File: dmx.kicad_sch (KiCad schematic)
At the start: 18 parts, among them J1 Conn_01x15_Socket, J2 Conn_01x04_Pin, J3 Conn_01x15_Socket, J5 Barrel_Jack_MountingPin, SW1 SW_Push, SW3 SW_Push

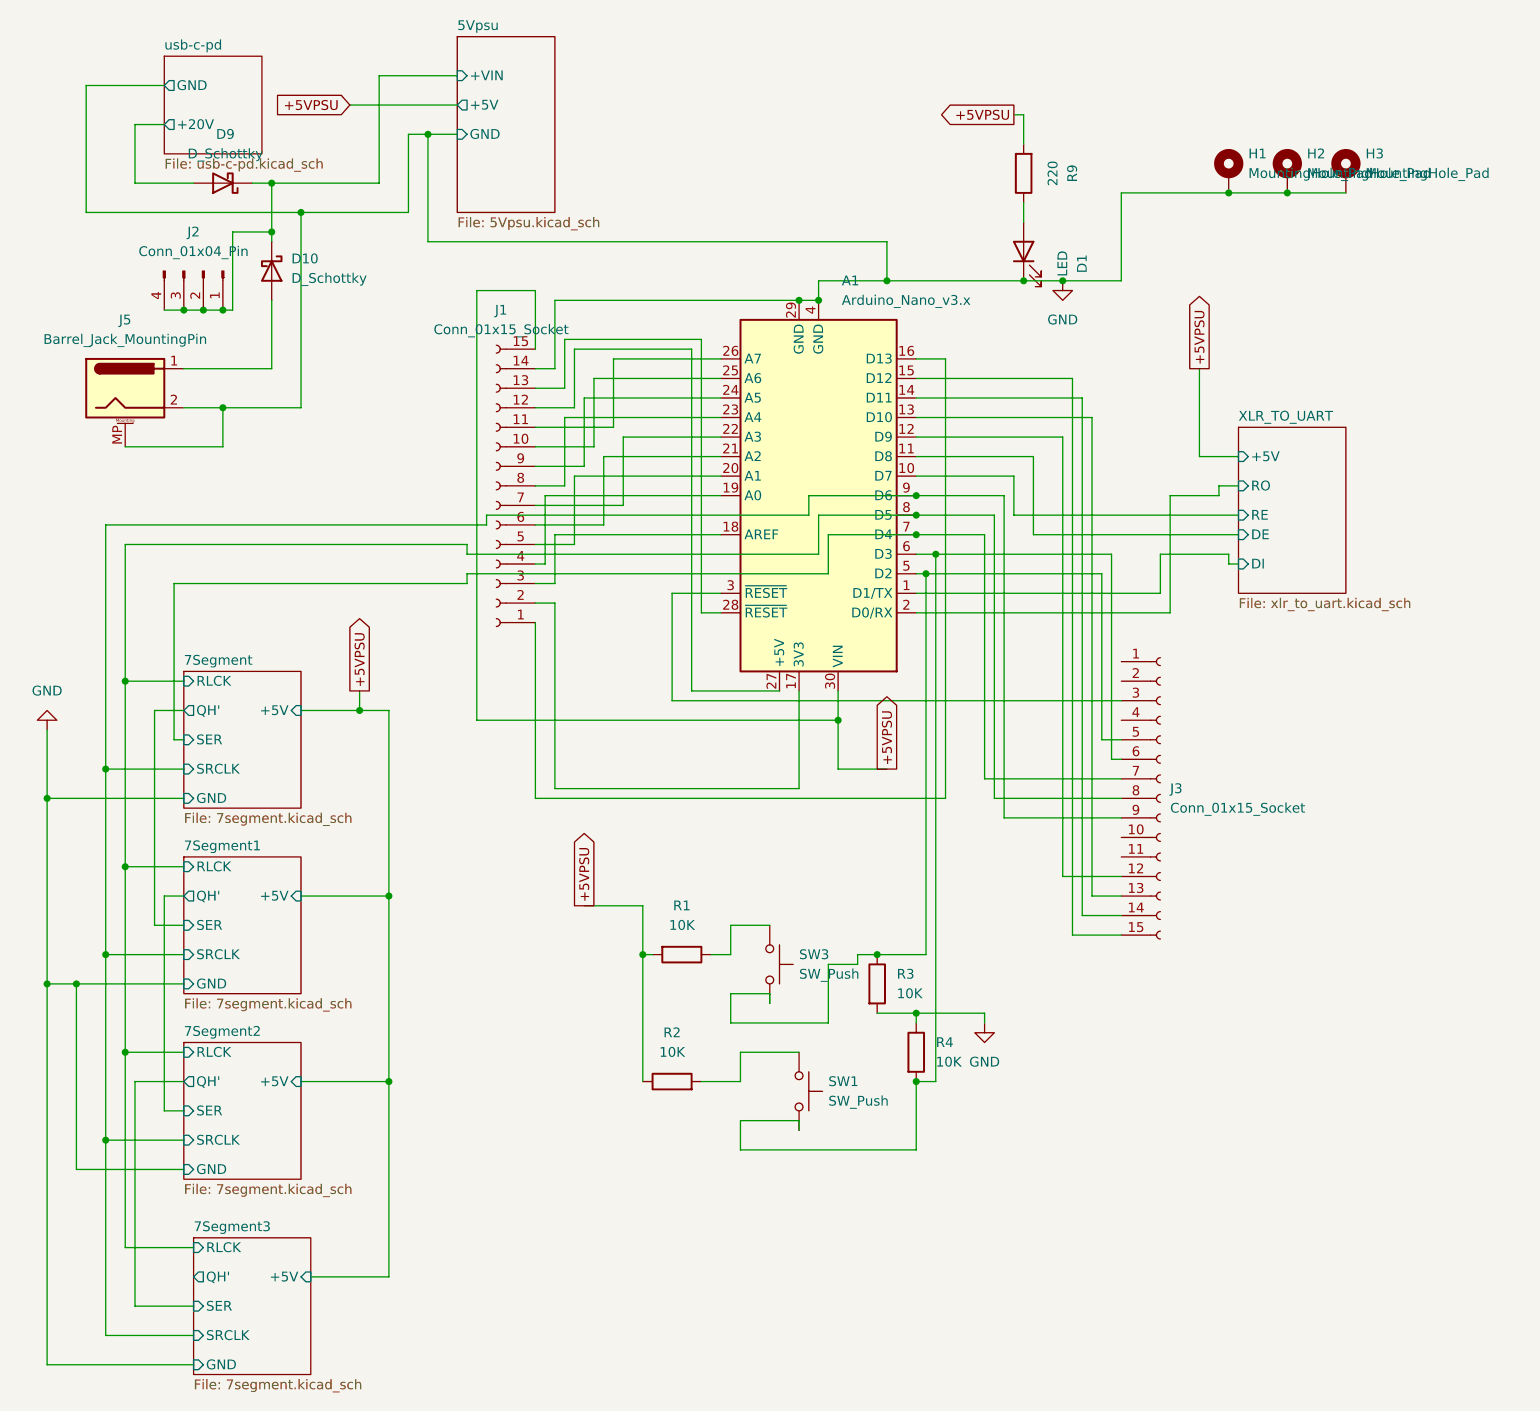
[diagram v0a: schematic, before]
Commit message: switch to cheaper components.
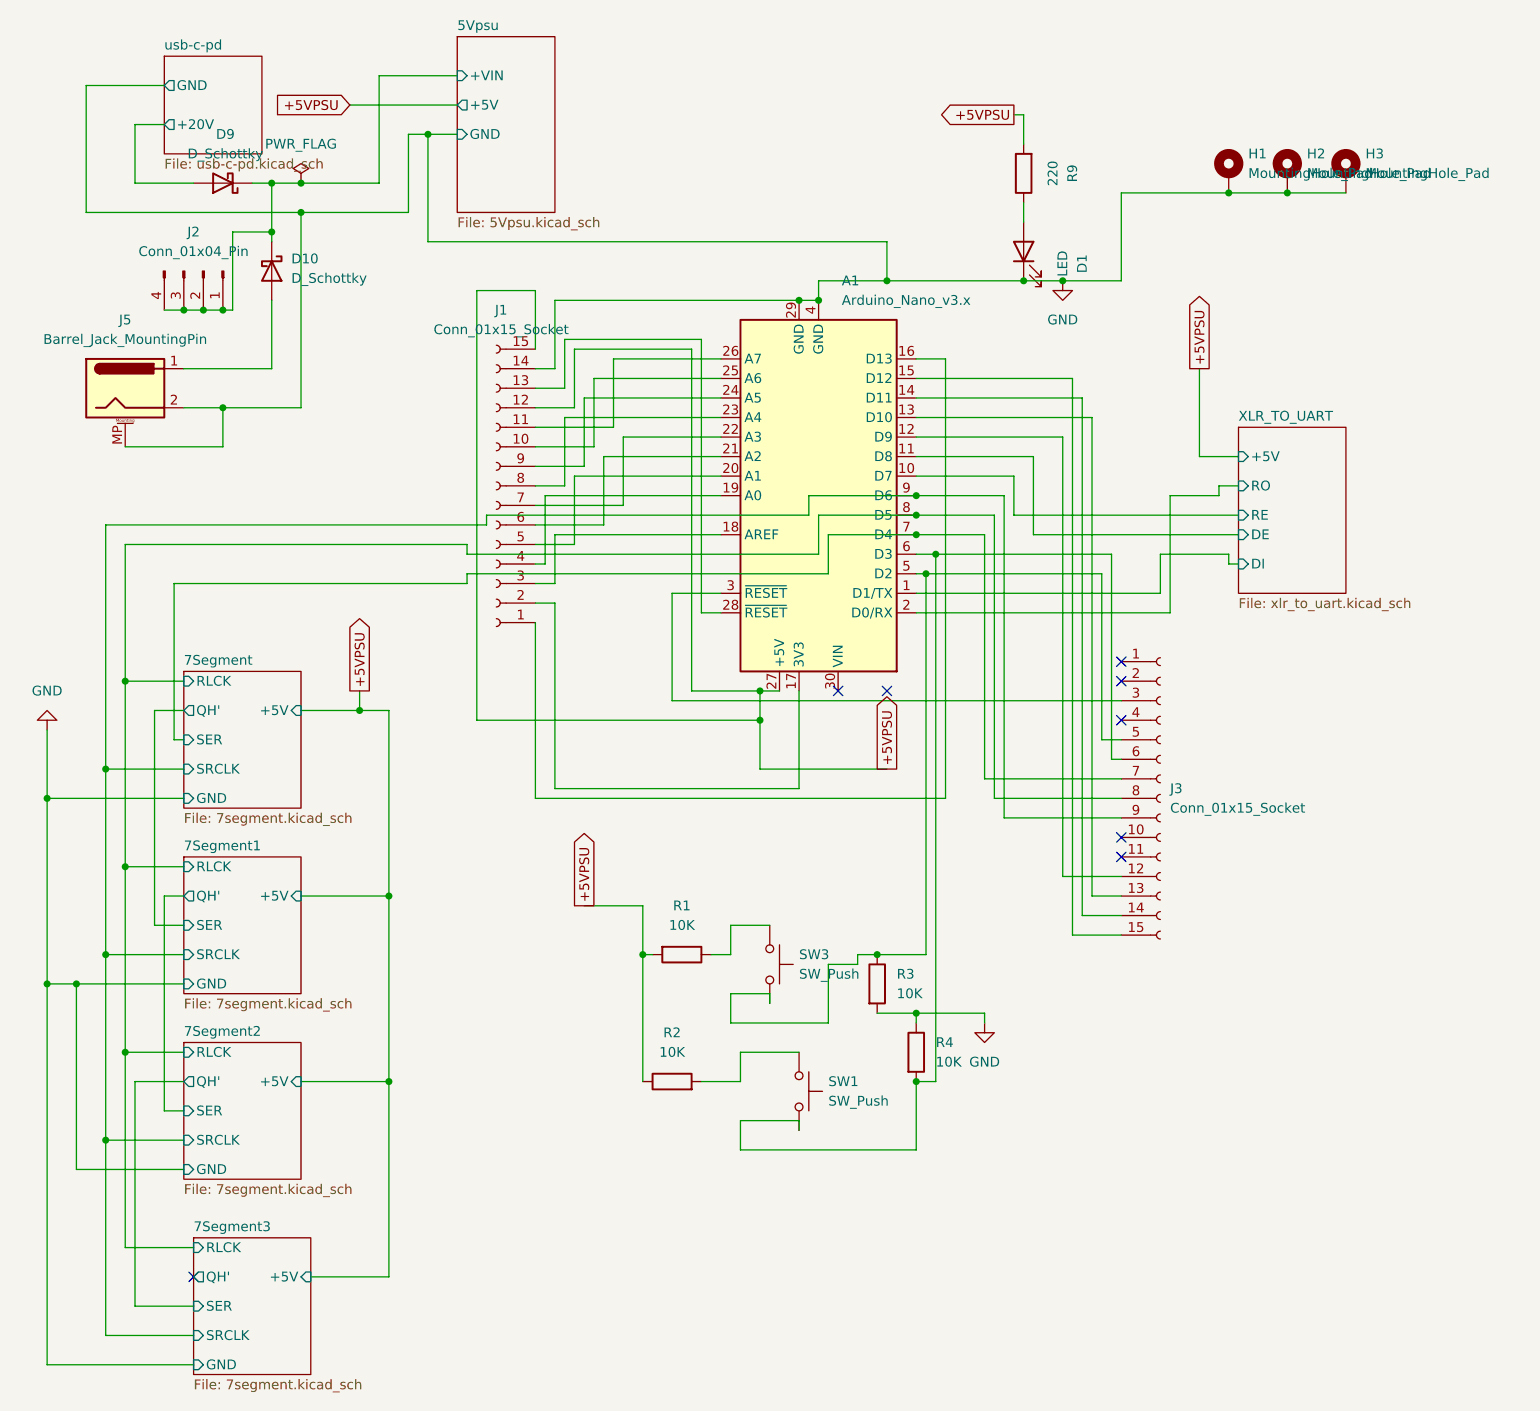
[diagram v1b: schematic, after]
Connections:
- net +5VPSU: now also A1.27 (+5V), J1.12 (Pin_12); no longer A1.30 (VIN)
- no-connect marks 0 -> 8
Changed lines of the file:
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@@
+	)
+	(junction
+		(at 111.76 109.22)
+		(diameter 0)
+		(color 0 0 0 0)
 	)
 	(junction
@@
 	)
 	(junction
+		(at 111.76 105.41)
+		(diameter 0)
+		(color 0 0 0 0)
+	)
+	(junction
 		(at 134.62 87.63)
 		(diameter 0)
@@
 	)
 	(junction
-		(at 121.92 109.22)
+		(at 52.07 39.37)
 		(diameter 0)
 		(color 0 0 0 0)
@@
 		(color 0 0 0 0)
 	)
+	(no_connect
+		(at 128.27 105.41)
+	)
+	(no_connect
+		(at 158.75 104.14)
+	)
+	(no_connect
+		(at 121.92 105.41)
+	)
+	(no_connect
+		(at 158.75 124.46)
+	)
+	(no_connect
+		(at 38.1 181.61)
+	)
+	(no_connect
+		(at 158.75 109.22)
+	)
+	(no_connect
+		(at 158.75 127)
+	)
+	(no_connect
+		(at 158.75 101.6)
+	)
 	(wire
 		(pts
@@
 	(wire
 		(pts
+			(xy 111.76 115.57) (xy 128.27 115.57)
+		)
+		(stroke
+			(width 0)
+			(type default)
+		)
+	)
+	(wire
+		(pts
 			(xy 19.05 143.51) (xy 19.05 119.38)
 		)
@@
 	(wire
 		(pts
-			(xy 74.93 109.22) (xy 121.92 109.22)
+			(xy 74.93 109.22) (xy 111.76 109.22)
 		)
 		(stroke
@@
 	(wire
 		(pts
-			(xy 121.92 109.22) (xy 121.92 115.57)
-		)
-		(stroke
-			(width 0)
-			(type default)
-		)
-	)
-	(wire
-		(pts
 			(xy 113.03 135.89) (xy 107.95 135.89)
 		)
@@
 	(wire
 		(pts
+			(xy 111.76 105.41) (xy 111.76 109.22)
+		)
+		(stroke
+			(width 0)
+			(type default)
+		)
+	)
+	(wire
+		(pts
 			(xy 120.65 148.59) (xy 120.65 140.97)
 		)
@@
 	(wire
 		(pts
+			(xy 52.07 39.37) (xy 62.23 39.37)
+		)
+		(stroke
+			(width 0)
+			(type default)
+		)
+	)
+	(wire
+		(pts
 			(xy 36.83 160.02) (xy 34.29 160.02)
 		)
@@
 	(wire
 		(pts
-			(xy 114.3 105.41) (xy 102.87 105.41)
+			(xy 114.3 105.41) (xy 111.76 105.41)
 		)
 		(stroke
@@
 	(wire
 		(pts
-			(xy 48.26 39.37) (xy 62.23 39.37)
+			(xy 48.26 39.37) (xy 52.07 39.37)
 		)
 		(stroke
@@
 	(wire
 		(pts
+			(xy 111.76 109.22) (xy 111.76 115.57)
+		)
+		(stroke
+			(width 0)
+			(type default)
+		)
+	)
+	(wire
+		(pts
 			(xy 172.72 87.63) (xy 163.83 87.63)
 		)
@@
 	(wire
 		(pts
-			(xy 121.92 115.57) (xy 128.27 115.57)
-		)
-		(stroke
-			(width 0)
-			(type default)
-		)
-	)
-	(wire
-		(pts
 			(xy 48.26 45.72) (xy 43.18 45.72)
 		)
@@
 	(wire
 		(pts
-			(xy 121.92 105.41) (xy 121.92 109.22)
+			(xy 111.76 105.41) (xy 102.87 105.41)
 		)
 		(stroke
@@
 					(unit 1)
 				)
+			)
+		)
+	)
+	(symbol
+		(lib_id "power:PWR_FLAG")
+		(at 52.07 39.37 0)
+		(unit 1)
+		(exclude_from_sim no)
+		(in_bom yes)
+		(on_board yes)
+		(dnp no)
+		(fields_autoplaced yes)
+		(property "Reference" "#FLG01"
+			(at 52.07 37.465 0)
+			(effects
+				(font
+					(size 1.27 1.27)
+				)
+				(hide yes)
+			)
+		)
+		(property "Value" "PWR_FLAG"
+			(at 52.07 34.29 0)
+			(effects
+				(font
+					(size 1.27 1.27)
+				)
+			)
+		)
+		(property "Footprint" ""
+			(at 52.07 39.37 0)
+			(effects
+				(font
+					(size 1.27 1.27)
+				)
+				(hide yes)
+			)
+		)
+		(property "Datasheet" "~"
+			(at 52.07 39.37 0)
+			(effects
+				(font
+					(size 1.27 1.27)
+				)
+				(hide yes)
+			)
+		)
+		(property "Description" "Special symbol for telling ERC where power comes from"
+			(at 52.07 39.37 0)
+			(effects
+				(font
+					(size 1.27 1.27)
+				)
+				(hide yes)
+			)
+		)
+		(pin "1"
+		)
+		(instances
+			(project "dmx"
+				(path "/860489ce-8e24-49a4-b6b1-5a2692123cd9"
+					(reference "#FLG01")
+					(unit 1)
+				)

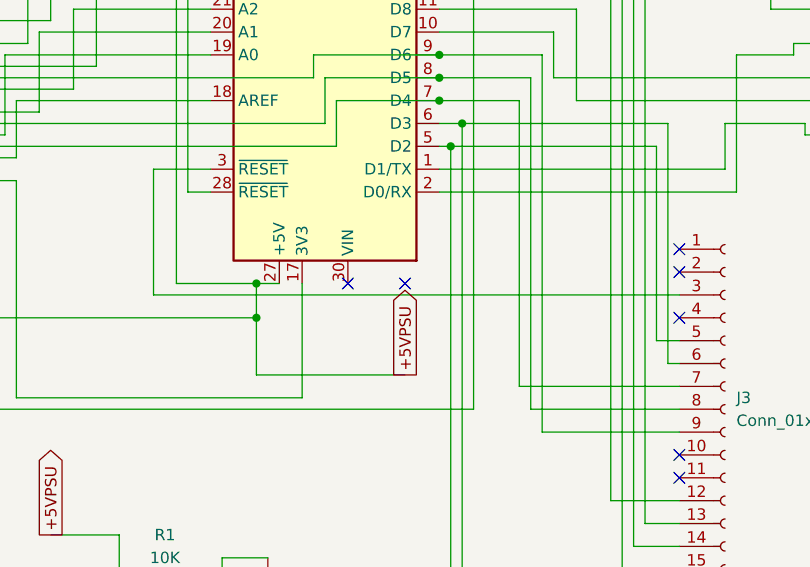
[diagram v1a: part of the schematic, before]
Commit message: replace extended components with basic components.
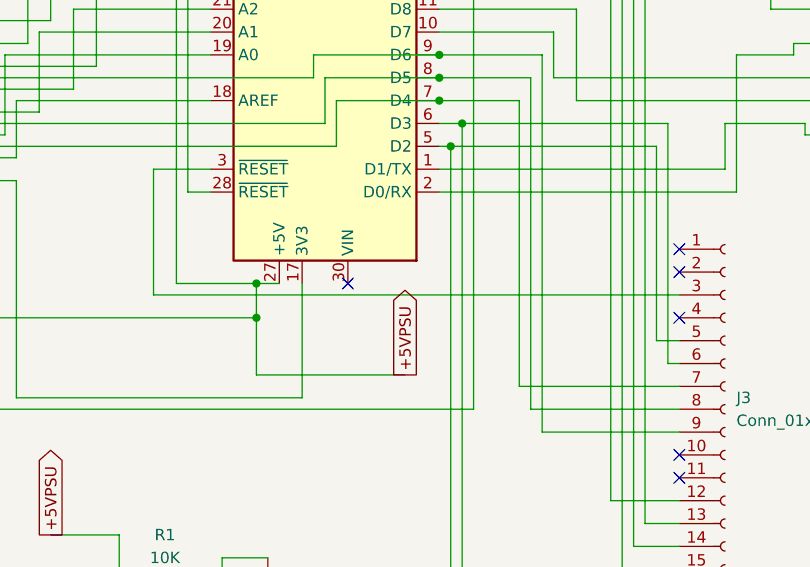
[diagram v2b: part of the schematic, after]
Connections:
- no-connect marks 8 -> 7
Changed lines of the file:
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@@
-	)
-	(no_connect
-		(at 128.27 105.41)
 	)
 	(no_connect

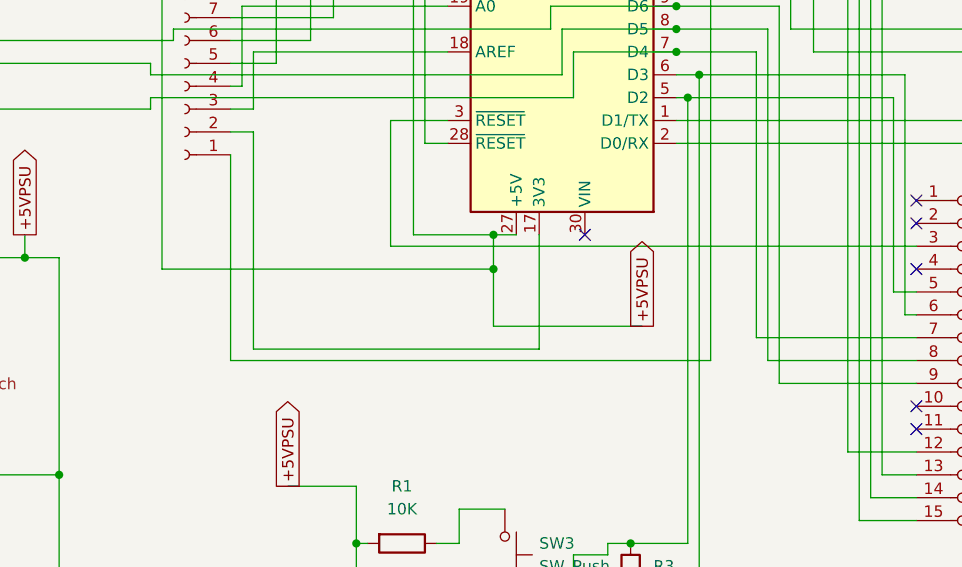
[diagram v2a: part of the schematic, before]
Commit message: add a +5V bridge to disbale the arduino
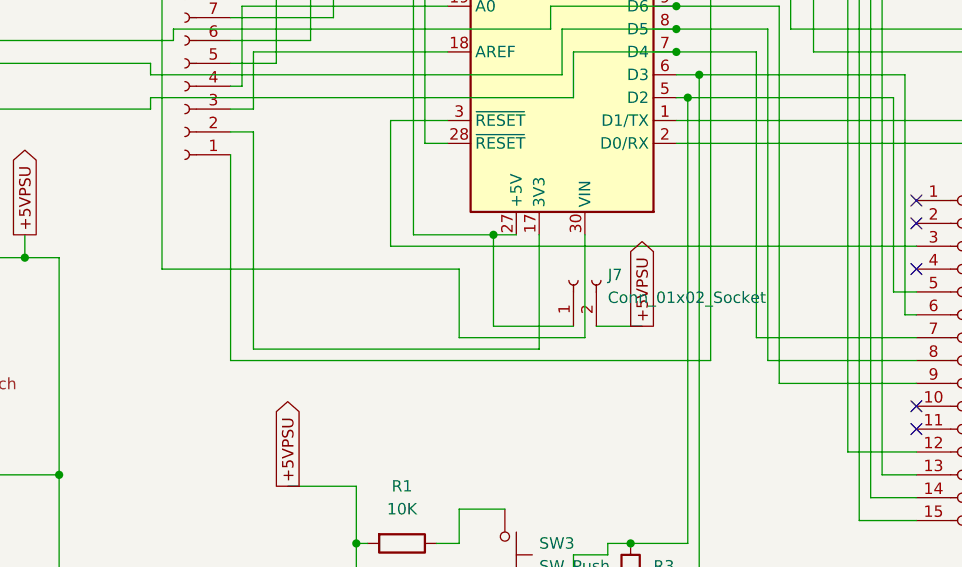
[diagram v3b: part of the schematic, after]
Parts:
- added J7: Conn_01x02_Socket, Connector_PinSocket_2.54mm:PinSocket_1x02_P2.54mm_Vertical, symbol Connector:Conn_01x02_Socket
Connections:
- net +5VPSU: now also J7.2 (Pin_2); no longer A1.27 (+5V), J1.12 (Pin_12), J1.15 (Pin_15)
- net at A1.30 (VIN): now also J1.15 (Pin_15)
- new net: A1.27 (+5V), J1.12 (Pin_12), J7.1 (Pin_1)
- no-connect marks 7 -> 6
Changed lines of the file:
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@@
 	)
 	(junction
-		(at 111.76 109.22)
-		(diameter 0)
-		(color 0 0 0 0)
-	)
-	(junction
 		(at 41.91 68.58)
 		(diameter 0)
@@
 	)
 	(no_connect
-		(at 121.92 105.41)
-	)
-	(no_connect
 		(at 158.75 124.46)
 	)
@@
 	(wire
 		(pts
-			(xy 111.76 115.57) (xy 128.27 115.57)
+			(xy 111.76 115.57) (xy 120.65 115.57)
 		)
 		(stroke
@@
 	(wire
 		(pts
+			(xy 123.19 115.57) (xy 128.27 115.57)
+		)
+		(stroke
+			(width 0)
+			(type default)
+		)
+	)
+	(wire
+		(pts
 			(xy 109.22 165.1) (xy 132.08 165.1)
 		)
@@
 	(wire
 		(pts
-			(xy 74.93 109.22) (xy 111.76 109.22)
+			(xy 74.93 109.22) (xy 107.95 109.22)
 		)
 		(stroke
@@
 	(wire
 		(pts
+			(xy 107.95 116.84) (xy 121.92 116.84)
+		)
+		(stroke
+			(width 0)
+			(type default)
+		)
+	)
+	(wire
+		(pts
 			(xy 22.86 143.51) (xy 19.05 143.51)
 		)
@@
 	(wire
 		(pts
-			(xy 111.76 105.41) (xy 111.76 109.22)
+			(xy 120.65 148.59) (xy 120.65 140.97)
 		)
 		(stroke
@@
 	(wire
 		(pts
-			(xy 120.65 148.59) (xy 120.65 140.97)
+			(xy 66.04 33.02) (xy 68.58 33.02)
 		)
 		(stroke
@@
 	(wire
 		(pts
-			(xy 66.04 33.02) (xy 68.58 33.02)
+			(xy 158.75 52.07) (xy 151.13 52.07)
 		)
 		(stroke
@@
 	(wire
 		(pts
-			(xy 158.75 52.07) (xy 151.13 52.07)
+			(xy 121.92 105.41) (xy 121.92 116.84)
 		)
 		(stroke
@@
 	(wire
 		(pts
+			(xy 107.95 109.22) (xy 107.95 116.84)
+		)
+		(stroke
+			(width 0)
+			(type default)
+		)
+	)
+	(wire
+		(pts
 			(xy 85.09 54.61) (xy 116.84 54.61)
 		)
@@
 	(wire
 		(pts
+			(xy 111.76 105.41) (xy 111.76 115.57)
+		)
+		(stroke
+			(width 0)
+			(type default)
+		)
+	)
+	(wire
+		(pts
 			(xy 157.48 114.3) (xy 158.75 114.3)
 		)
@@
 	(wire
 		(pts
-			(xy 111.76 109.22) (xy 111.76 115.57)
-		)
-		(stroke
-			(width 0)
-			(type default)
-		)
-	)
-	(wire
-		(pts
 			(xy 172.72 87.63) (xy 163.83 87.63)
 		)
@@
 					(unit 1)
 				)
+			)
+		)
+	)
+	(symbol
+		(lib_id "Connector:Conn_01x02_Socket")
+		(at 120.65 110.49 90)
+		(unit 1)
+		(exclude_from_sim no)
+		(in_bom yes)
+		(on_board yes)
+		(dnp no)
+		(fields_autoplaced yes)
+		(property "Reference" "J7"
+			(at 124.46 109.8549 90)
+			(effects
+				(font
+					(size 1.27 1.27)
+				)
+				(justify right)
+			)
+		)
+		(property "Value" "Conn_01x02_Socket"
+			(at 124.46 112.3949 90)
+			(effects
+				(font
+					(size 1.27 1.27)
+				)
+				(justify right)
+			)
+		)
+		(property "Footprint" "Connector_PinSocket_2.54mm:PinSocket_1x02_P2.54mm_Vertical"
+			(at 120.65 110.49 0)
+			(effects
+				(font
+					(size 1.27 1.27)
+				)
+				(hide yes)
+			)
+		)
+		(property "Datasheet" "~"
+			(at 120.65 110.49 0)
+			(effects
+				(font
+					(size 1.27 1.27)
+				)
+				(hide yes)
+			)
+		)
+		(property "Description" "Generic connector, single row, 01x02, script generated"
+			(at 120.65 110.49 0)
+			(effects
+				(font
+					(size 1.27 1.27)
+				)
+				(hide yes)
+			)
+		)
+		(pin "1"
+		)
+		(pin "2"
+		)
+		(instances
+			(project "dmx"
+				(path "/860489ce-8e24-49a4-b6b1-5a2692123cd9"
+					(reference "J7")
+					(unit 1)
+				)
